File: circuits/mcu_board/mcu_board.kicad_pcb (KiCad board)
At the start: 2 copper layers, 96.3 x 62.6 mm, 44 parts, among them J1 USB_B_Micro, J2 Conn_01x13_Pin, J3 Conn_01x03_Pin, SW1 SW_Push, SW10 SW_Push, SW11 SW_Push, SW12 SW_Push, SW13 SW_Push, SW2 SW_Push, SW3 SW_Push, SW4 SW_Push, SW5 SW_Push, SW6 SW_Push, SW7 SW_Push, SW8 SW_Push, SW9 SW_Push, U1 AMS1117-3.3, U4 STM32F302CCTx, Y1 8MHz

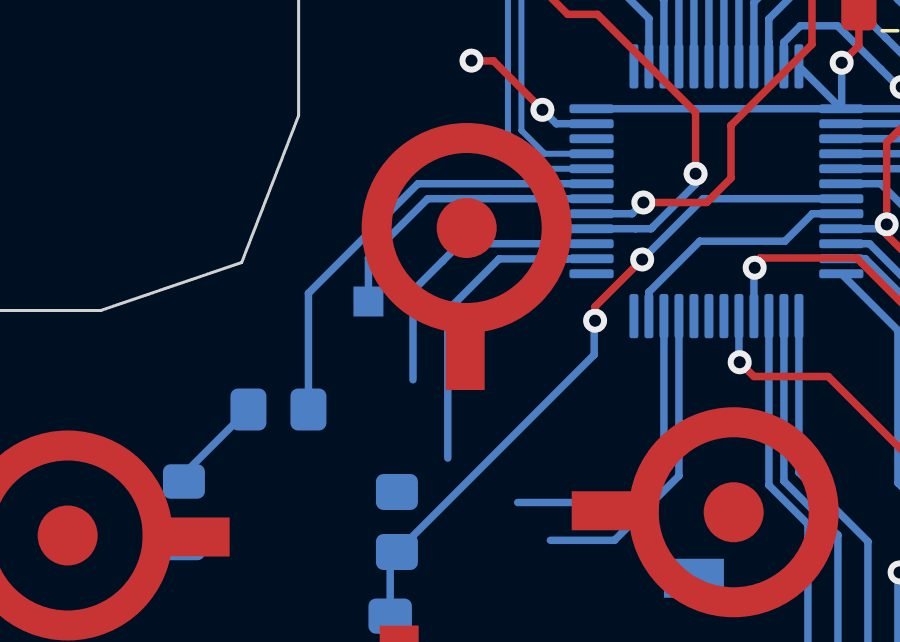
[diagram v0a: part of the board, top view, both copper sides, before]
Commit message: 按键逻辑修改完成,未测试
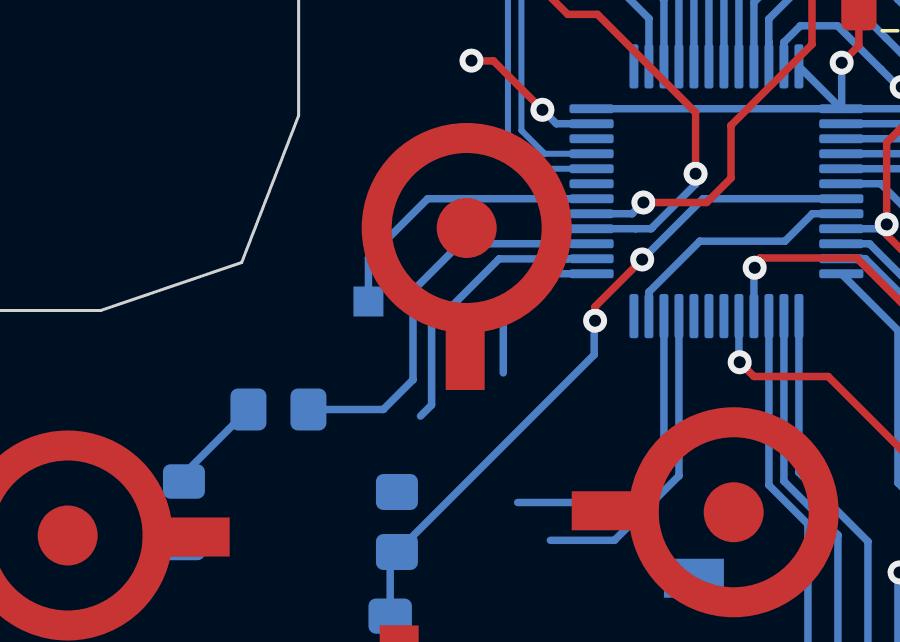
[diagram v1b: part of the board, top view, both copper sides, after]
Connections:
- U4 pad 25: /PB12 -> /BTN_UP
- U4 pad 26: /BTN_UP -> /BTN_LEFT
- U4 pad 27: /BTN_LEFT -> /LED1
- U4 pad 31: /LED1 -> unconnected-(U4-PA10-Pad31)
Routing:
- net /BTN_UP: track 10.4 -> 5.65 mm
- net /LED1: track 14.8 -> 13.5 mm
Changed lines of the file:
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@@
   (net 46 "/PB1")
   (net 47 "/PB2")
-  (net 48 "/PB12")
+  (net 48 "unconnected-(U4-PA10-Pad31)")
   (footprint "button:touch" (layer "F.Cu")
     (at 174.52625 100.16)
@@
       (net 4 "+3V3") (pinfunction "VDD") (pintype "power_in"))
     (pad "25" smd roundrect (at 4.1625 -2.75 180) (size 1.475 0.3) (layers "B.Cu" "B.Paste" "B.Mask") (roundrect_rratio 0.25)
-      (net 48 "/PB12") (pinfunction "PB12") (pintype "bidirectional+no_connect"))
+      (net 33 "/BTN_UP") (pinfunction "PB12") (pintype "bidirectional"))
     (pad "26" smd roundrect (at 4.1625 -2.25 180) (size 1.475 0.3) (layers "B.Cu" "B.Paste" "B.Mask") (roundrect_rratio 0.25)
-      (net 33 "/BTN_UP") (pinfunction "PB13") (pintype "bidirectional"))
+      (net 36 "/BTN_LEFT") (pinfunction "PB13") (pintype "bidirectional"))
     (pad "27" smd roundrect (at 4.1625 -1.75 180) (size 1.475 0.3) (layers "B.Cu" "B.Paste" "B.Mask") (roundrect_rratio 0.25)
-      (net 36 "/BTN_LEFT") (pinfunction "PB14") (pintype "bidirectional"))
+      (net 42 "/LED1") (pinfunction "PB14") (pintype "bidirectional"))
     (pad "28" smd roundrect (at 4.1625 -1.25 180) (size 1.475 0.3) (layers "B.Cu" "B.Paste" "B.Mask") (roundrect_rratio 0.25)
       (net 41 "/BTN_PAIR") (pinfunction "PB15") (pintype "bidirectional"))
@@
       (net 25 "/UART_TX") (pinfunction "PA9") (pintype "bidirectional"))
     (pad "31" smd roundrect (at 4.1625 0.25 180) (size 1.475 0.3) (layers "B.Cu" "B.Paste" "B.Mask") (roundrect_rratio 0.25)
-      (net 42 "/LED1") (pinfunction "PA10") (pintype "bidirectional"))
+      (net 48 "unconnected-(U4-PA10-Pad31)") (pinfunction "PA10") (pintype "bidirectional+no_connect"))
     (pad "32" smd roundrect (at 4.1625 0.75 180) (size 1.475 0.3) (layers "B.Cu" "B.Paste" "B.Mask") (roundrect_rratio 0.25)
       (net 32 "/MCU_D-") (pinfunction "PA11") (pintype "bidirectional"))
@@
   (segment (start 154.8 91.025) (end 154.8 91.275) (width 0.2) (layer "B.Cu") (net 32))
   (segment (start 155.599999 94.206801) (end 153.7818 96.025) (width 0.2) (layer "B.Cu") (net 32))
-  (segment (start 146.0625 115.575) (end 145.259315 115.575) (width 0.25) (layer "B.Cu") (net 33))
-  (segment (start 145.254315 115.58) (end 142.98 115.58) (width 0.25) (layer "B.Cu") (net 33))
-  (segment (start 141.27 117.29) (end 141.27 122.22) (width 0.25) (layer "B.Cu") (net 33))
-  (segment (start 145.259315 115.575) (end 145.254315 115.58) (width 0.25) (layer "B.Cu") (net 33))
-  (segment (start 142.98 115.58) (end 141.27 117.29) (width 0.25) (layer "B.Cu") (net 33))
+  (segment (start 143.12 117.1) (end 143.12 119.38) (width 0.25) (layer "B.Cu") (net 33))
+  (segment (start 143.21 117.01) (end 143.12 117.1) (width 0.25) (layer "B.Cu") (net 33))
+  (segment (start 146.0625 116.075) (end 144.145 116.075) (width 0.25) (layer "B.Cu") (net 33))
+  (segment (start 144.145 116.075) (end 143.21 117.01) (width 0.25) (layer "B.Cu") (net 33))
   (segment (start 154.47 103.13) (end 153.41 104.19) (width 0.25) (layer "F.Cu") (net 34))
   (segment (start 153.41 104.19) (end 153.41 108.43) (width 0.25) (layer "F.Cu") (net 34))
@@
   (segment (start 148.975 122.811396) (end 146.826396 124.96) (width 0.25) (layer "B.Cu") (net 35))
   (segment (start 146.826396 124.96) (end 144.69 124.96) (width 0.25) (layer "B.Cu") (net 35))
-  (segment (start 146.0625 115.075) (end 145.259315 115.075) (width 0.25) (layer "B.Cu") (net 36))
-  (segment (start 140.11 116.64) (end 140.11 119.61) (width 0.25) (layer "B.Cu") (net 36))
-  (segment (start 141.09 115.66) (end 140.11 116.64) (width 0.25) (layer "B.Cu") (net 36))
-  (segment (start 145.259315 115.075) (end 141.675 115.075) (width 0.25) (layer "B.Cu") (net 36))
-  (segment (start 141.675 115.075) (end 141.09 115.66) (width 0.25) (layer "B.Cu") (net 36))
+  (segment (start 146.0625 115.575) (end 145.259315 115.575) (width 0.25) (layer "B.Cu") (net 36))
+  (segment (start 145.254315 115.58) (end 142.98 115.58) (width 0.25) (layer "B.Cu") (net 36))
+  (segment (start 141.27 117.29) (end 140.73 117.83) (width 0.25) (layer "B.Cu") (net 36))
+  (segment (start 140.73 117.83) (end 140.73 117.84) (width 0.25) (layer "B.Cu") (net 36))
+  (segment (start 145.259315 115.575) (end 145.254315 115.58) (width 0.25) (layer "B.Cu") (net 36))
+  (segment (start 140.73 117.84) (end 140.73 120.45) (width 0.25) (layer "B.Cu") (net 36))
+  (segment (start 140.73 120.45) (end 140.36 120.82) (width 0.25) (layer "B.Cu") (net 36))
+  (segment (start 142.98 115.58) (end 141.27 117.29) (width 0.25) (layer "B.Cu") (net 36))
   (segment (start 148.475 117.4875) (end 148.475 122.675) (width 0.25) (layer "B.Cu") (net 37))
   (segment (start 147.45 123.7) (end 143.6 123.7) (width 0.25) (layer "B.Cu") (net 37))
@@
   (segment (start 148.045 114.575) (end 148.1 114.52) (width 0.25) (layer "B.Cu") (net 41))
   (segment (start 147.535 114.575) (end 148.045 114.575) (width 0.25) (layer "B.Cu") (net 41))
-  (segment (start 140.275 113.075) (end 136.625 116.725) (width 0.25) (layer "B.Cu") (net 42))
-  (segment (start 136.625 116.725) (end 136.625 120.6) (width 0.25) (layer "B.Cu") (net 42))
-  (segment (start 146.0625 113.075) (end 140.275 113.075) (width 0.25) (layer "B.Cu") (net 42))
+  (segment (start 139.12 120.6) (end 136.625 120.6) (width 0.25) (layer "B.Cu") (net 42))
+  (segment (start 140.11 119.61) (end 139.12 120.6) (width 0.25) (layer "B.Cu") (net 42))
+  (segment (start 146.0625 115.075) (end 141.675 115.075) (width 0.25) (layer "B.Cu") (net 42))
+  (segment (start 141.675 115.075) (end 140.11 116.64) (width 0.25) (layer "B.Cu") (net 42))
+  (segment (start 140.11 116.64) (end 140.11 119.61) (width 0.25) (layer "B.Cu") (net 42))
   (segment (start 152.46 104.82) (end 152.46 102.6) (width 0.25) (layer "F.Cu") (net 43))
   (segment (start 152.46 102.6) (end 152.6 102.46) (width 0.25) (layer "F.Cu") (net 43))

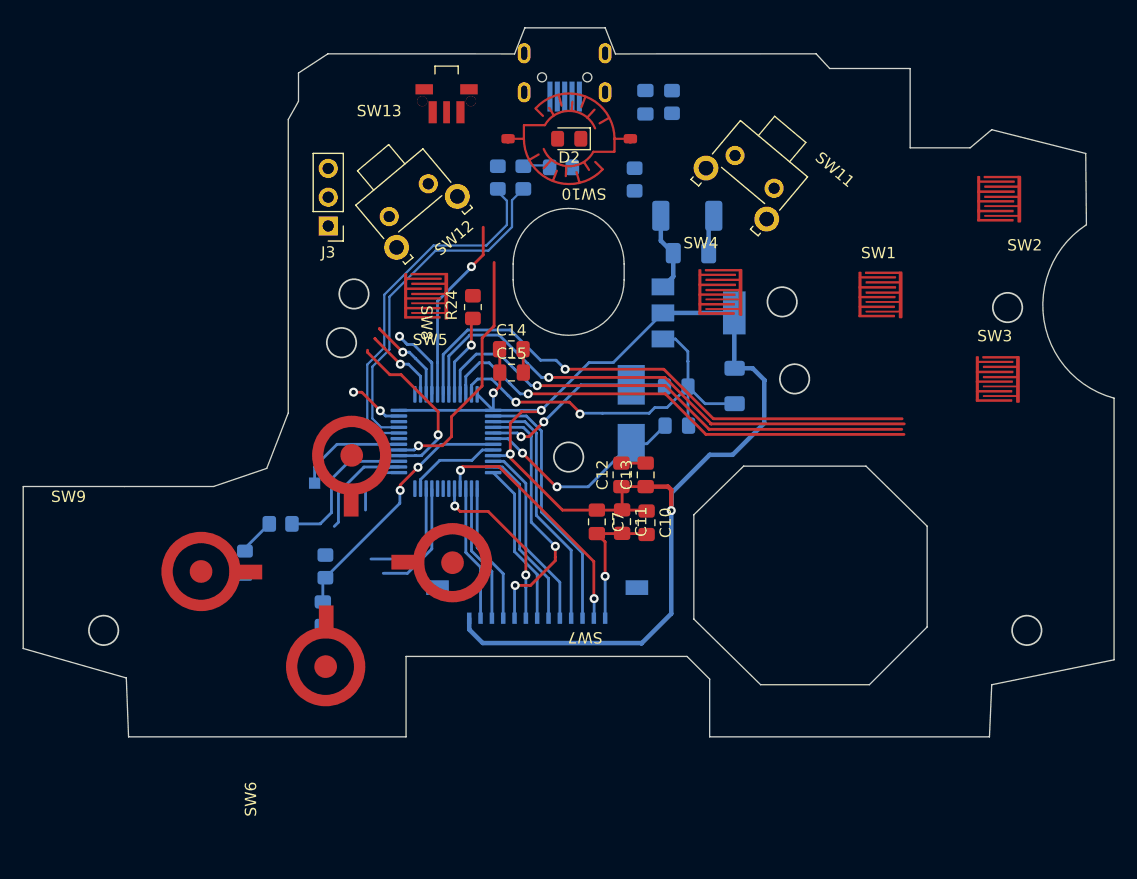
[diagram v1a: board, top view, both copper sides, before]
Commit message: layout mcu板边界优化
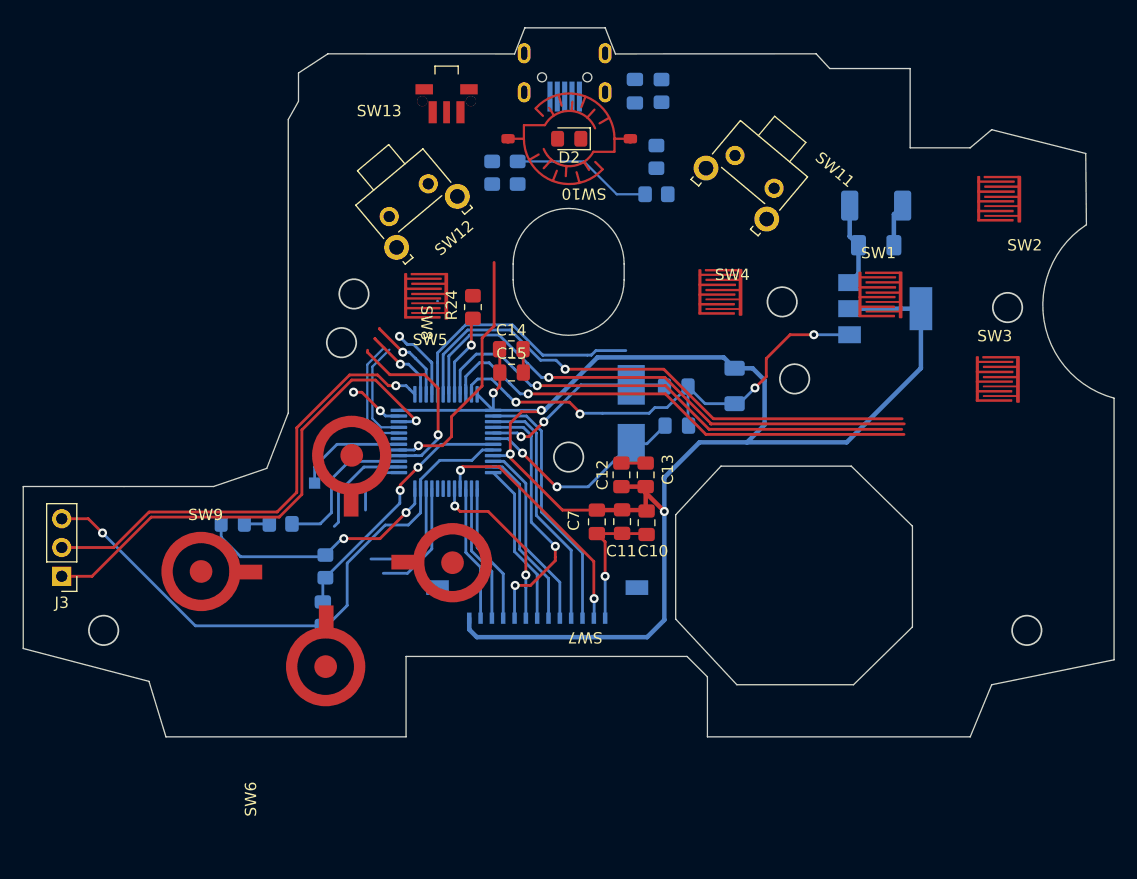
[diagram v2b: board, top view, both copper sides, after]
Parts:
- moved J3 38.9 mm to (116.3, 125.2)
- moved D1 16.7 mm to (188.2, 92.5)
- moved U1 16.5 mm to (189.0, 101.6)
- moved C2 16.4 mm to (188.2, 96.0)
- moved R10 8.75 mm to (168.8, 91.5)
- moved D3 3.59 mm to (131.4, 120.6), turned to 180 degrees
- moved R13 2.78 mm to (168.8, 88.2)
- moved R1 1.34 mm to (169.2, 82.4)
- moved C1 1.34 mm to (166.9, 82.4)
- moved R11 0.66 mm to (156.6, 89.6)
- moved R12 0.66 mm to (154.3, 89.6)
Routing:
- net GND: track 69.6 -> 121.8 mm, vias 5 -> 8
- net +3V3: track 124.7 -> 170.1 mm, vias 4 -> 6
- net /SWDIO: track 0.00 -> 44.9 mm, vias 0 -> 1
- net /SWCLK: track 0.00 -> 41.5 mm, vias 0 -> 1
- net /MCU_D+: track 31.2 -> 9.36 mm
- net /MCU_D-: track 31.8 -> 10.3 mm
- net /D+: track 2.52 -> 12.5 mm
- net /BTN_RB: track 16.4 -> 22.6 mm, vias 1 -> 0
- net /BTN_PAIR: track 15.1 -> 16.3 mm
- net Net-(D3-K): track 3.29 -> 2.20 mm
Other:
- outline, holes or cut-outs redrawn

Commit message: 螺丝孔位置确定，xbox键位置确定
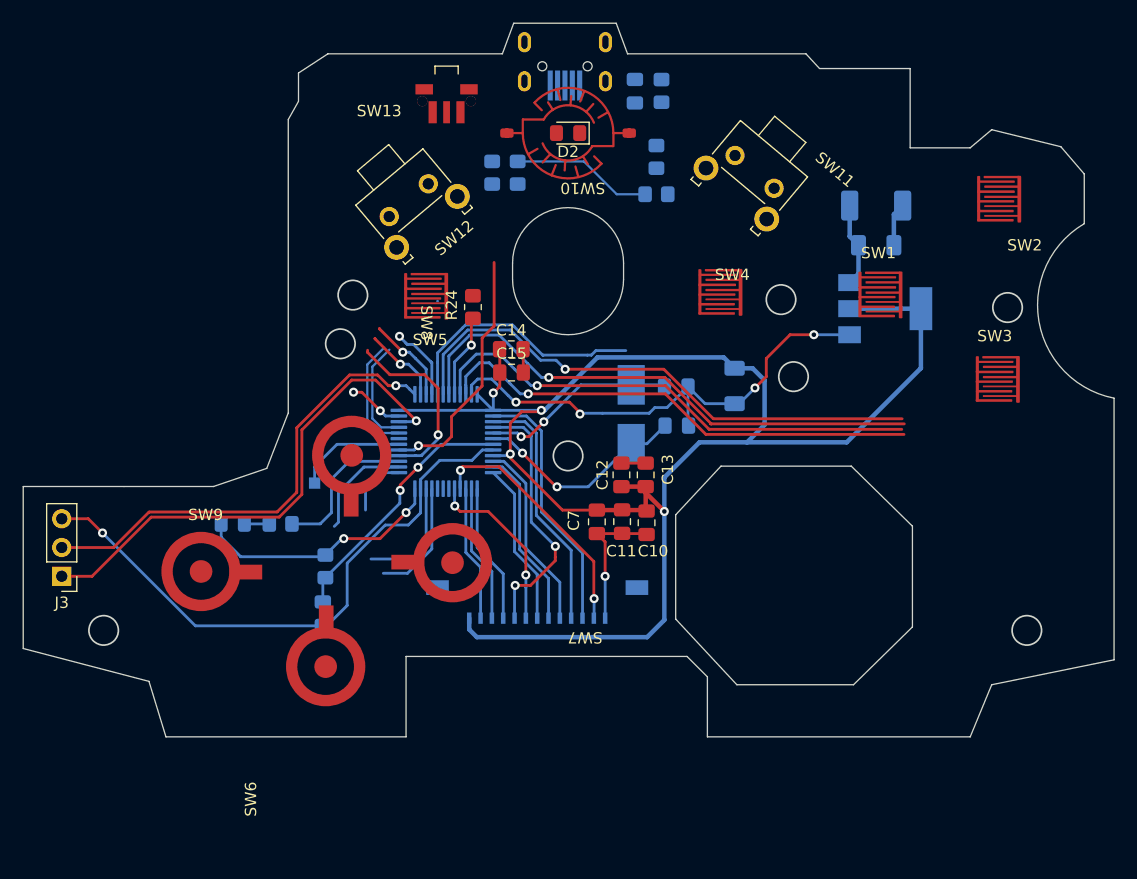
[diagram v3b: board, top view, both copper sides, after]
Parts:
- moved J1 0.98 mm to (160.7, 79.0)
- moved D2 0.51 mm to (161.0, 86.1)
- moved SW10 0.51 mm to (161.0, 86.1)
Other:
- board size 96.3 x 62.6 mm -> 96.3 x 63 mm
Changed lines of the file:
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@@
   (setup
     (pad_to_mask_clearance 0)
-    (aux_axis_origin 110.1 105)
+    (aux_axis_origin 109.83 141.78)
     (pcbplotparams
       (layerselection 0x00010fc_ffffffff)
@@
   )
   (footprint "LED_SMD:LED_0805_2012Metric_Pad1.15x1.40mm_HandSolder" (layer "F.Cu")
-    (at 161.1 86.600001 180)
+    (at 161 86.1 180)
     (descr "LED SMD 0805 (2012 Metric), square (rectangular) end terminal, IPC_7351 nominal, (Body size source: https://docs.google.com/spreadsheets/d/1BsfQQcO9C6DZCsRaXUlFlo91Tg2WpOkGARC1WS5S8t0/edit?usp=sharing), generated with kicad-footprint-generator")
     (tags "LED handsolder")
@@
   )
   (footprint "button:touch-xbox" (layer "F.Cu")
-    (at 161.1 86.6 180)
+    (at 161 86.1 180)
     (property "Sheetfile" "mcu_board.kicad_sch")
     (property "Sheetname" "")
@@
   )
   (footprint "usb_micro:USB_MICRO" (layer "B.Cu")
-    (at 160.7 80)
+    (at 160.725 79.025)
     (property "Sheetfile" "mcu_board.kicad_sch")
     (property "Sheetname" "")
@@
   (gr_line (start 186 115.5) (end 174.5 115.5)
     (stroke (width 0.1) (type default)) (layer "Edge.Cuts"))
-  (gr_line (start 165.95 99.05) (end 165.95 97.65)
+  (gr_line (start 165.9 99) (end 165.9 97.58)
     (stroke (width 0.1) (type default)) (layer "Edge.Cuts"))
   (gr_line (start 174.5 115.5) (end 170.5 119.8)
     (stroke (width 0.1) (type default)) (layer "Edge.Cuts"))
-  (gr_line (start 184.1 80.4) (end 182.9 79.1)
+  (gr_line (start 183.2 80.4) (end 182 79.1)
     (stroke (width 0.1) (type default)) (layer "Edge.Cuts"))
   (gr_line (start 146.7 132.3) (end 146.7 139.4)
@@
   (gr_line (start 209.2 109.5) (end 209.2 132.6)
     (stroke (width 0.1) (type default)) (layer "Edge.Cuts"))
-  (gr_line (start 156.15 97.65) (end 156.15 99.05)
-    (stroke (width 0.1) (type default)) (layer "Edge.Cuts"))
-  (gr_arc (start 156.15 97.65) (mid 161.05 92.75) (end 165.95 97.65)
+  (gr_line (start 156.1 97.58) (end 156.1 99)
+    (stroke (width 0.1) (type default)) (layer "Edge.Cuts"))
+  (gr_arc (start 156.1 97.58) (mid 161 92.68) (end 165.9 97.58)
     (stroke (width 0.1) (type default)) (layer "Edge.Cuts"))
   (gr_circle (center 201.5 130) (end 202.8 130)
@@
   (gr_line (start 191.4 120.8) (end 186 115.5)
     (stroke (width 0.1) (type default)) (layer "Edge.Cuts"))
-  (gr_line (start 206.7 87.9) (end 198.4 85.8)
+  (gr_line (start 155.2 79.1) (end 156.2 76.4)
+    (stroke (width 0.1) (type default)) (layer "Edge.Cuts"))
+  (gr_line (start 204.5 87.3) (end 198.4 85.8)
     (stroke (width 0.1) (type default)) (layer "Edge.Cuts"))
   (gr_line (start 137.2 80.8) (end 139.8 79.1)
@@
   (gr_line (start 209.2 132.6) (end 198.4 134.8)
     (stroke (width 0.1) (type default)) (layer "Edge.Cuts"))
-  (gr_circle (center 181 107.8) (end 182.3 107.8)
+  (gr_circle (center 180.9 107.6) (end 182.2 107.6)
     (stroke (width 0.15) (type default)) (fill none) (layer "Edge.Cuts"))
   (gr_line (start 125.5 139.4) (end 124 134.5)
     (stroke (width 0.1) (type default)) (layer "Edge.Cuts"))
-  (gr_circle (center 161.05 114.7) (end 162.35 114.7)
+  (gr_circle (center 161 114.6) (end 162.3 114.6)
     (stroke (width 0.15) (type default)) (fill none) (layer "Edge.Cuts"))
-  (gr_line (start 165.18 79.11) (end 164.28 76.81)
-    (stroke (width 0.1) (type default)) (layer "Edge.Cuts"))
   (gr_line (start 173.3 139.4) (end 173.3 134.1)
     (stroke (width 0.1) (type default)) (layer "Edge.Cuts"))
@@
   (gr_line (start 121.8 117.3) (end 129.7 117.3)
     (stroke (width 0.1) (type default)) (layer "Edge.Cuts"))
-  (gr_line (start 156.28 79.11) (end 157.18 76.81)
-    (stroke (width 0.1) (type default)) (layer "Edge.Cuts"))
-  (gr_circle (center 141 104.6) (end 142.3 104.6)
+  (gr_circle (center 140.9 104.7) (end 142.2 104.7)
     (stroke (width 0.15) (type default)) (fill none) (layer "Edge.Cuts"))
   (gr_circle (center 199.8 101.5) (end 201.1 101.5)
     (stroke (width 0.15) (type default)) (fill none) (layer "Edge.Cuts"))
-  (gr_line (start 157.18 76.81) (end 164.28 76.81)
+  (gr_line (start 156.2 76.4) (end 165.25 76.4)
     (stroke (width 0.1) (type default)) (layer "Edge.Cuts"))
   (gr_line (start 173.3 134.1) (end 171.5 132.3)
@@
   (gr_line (start 196.5 87.4) (end 191.2 87.4)
     (stroke (width 0.1) (type default)) (layer "Edge.Cuts"))
-  (gr_circle (center 142.1 100.3) (end 143.4 100.3)
+  (gr_circle (center 142 100.4) (end 143.3 100.4)
     (stroke (width 0.15) (type default)) (fill none) (layer "Edge.Cuts"))
+  (gr_arc (start 209.2 109.5) (mid 202.564285 102.704634) (end 206.572431 94.093916)
+    (stroke (width 0.1) (type default)) (layer "Edge.Cuts"))
   (gr_line (start 196.5 139.4) (end 198.4 134.8)
     (stroke (width 0.1) (type default)) (layer "Edge.Cuts"))
   (gr_line (start 146.7 139.4) (end 125.5 139.4)
     (stroke (width 0.1) (type default)) (layer "Edge.Cuts"))
-  (gr_line (start 139.8 79.1) (end 156.28 79.11)
+  (gr_line (start 166.25 79.1) (end 165.25 76.4)
+    (stroke (width 0.1) (type default)) (layer "Edge.Cuts"))
+  (gr_line (start 139.8 79.1) (end 155.2 79.1)
     (stroke (width 0.1) (type default)) (layer "Edge.Cuts"))
   (gr_line (start 191.4 129.7) (end 191.4 120.8)
     (stroke (width 0.1) (type default)) (layer "Edge.Cuts"))
-  (gr_arc (start 209.2 109.5) (mid 203.015895 102.636707) (end 206.759178 94.190656)
-    (stroke (width 0.1) (type default)) (layer "Edge.Cuts"))
-  (gr_circle (center 179.9 101) (end 181.2 101)
+  (gr_circle (center 179.8 100.8) (end 181.1 100.8)
     (stroke (width 0.15) (type default)) (fill none) (layer "Edge.Cuts"))
   (gr_line (start 171.5 132.3) (end 146.7 132.3)
@@
   (gr_line (start 191.4 129.7) (end 186.2 134.8)
     (stroke (width 0.1) (type default)) (layer "Edge.Cuts"))
-  (gr_line (start 191.2 80.4) (end 184.1 80.4)
-    (stroke (width 0.1) (type default)) (layer "Edge.Cuts"))
-  (gr_line (start 182.9 79.1) (end 165.18 79.11)
+  (gr_line (start 206.572431 94.093916) (end 206.57 89.71)
+    (stroke (width 0.1) (type default)) (layer "Edge.Cuts"))
+  (gr_line (start 191.2 80.4) (end 183.2 80.4)
+    (stroke (width 0.1) (type default)) (layer "Edge.Cuts"))
+  (gr_line (start 182 79.1) (end 166.25 79.1)
     (stroke (width 0.1) (type default)) (layer "Edge.Cuts"))
   (gr_line (start 129.7 117.3) (end 134.4 115.7)
@@
   (gr_circle (center 120 130) (end 121.3 130)
     (stroke (width 0.15) (type default)) (fill none) (layer "Edge.Cuts"))
-  (gr_line (start 206.759178 94.190656) (end 206.7 87.9)
-    (stroke (width 0.1) (type default)) (layer "Edge.Cuts"))
-  (gr_arc (start 165.95 99.05) (mid 161.05 103.95) (end 156.15 99.05)
+  (gr_arc (start 165.9 99) (mid 161 103.9) (end 156.1 99)
     (stroke (width 0.1) (type default)) (layer "Edge.Cuts"))
   (gr_line (start 124 134.5) (end 112.9 131.6)
     (stroke (width 0.1) (type default)) (layer "Edge.Cuts"))
+  (gr_line (start 204.5 87.3) (end 206.57 89.71)
+    (stroke (width 0.1) (type default)) (layer "Edge.Cuts"))
   (gr_line (start 198.4 85.8) (end 196.5 87.4)
